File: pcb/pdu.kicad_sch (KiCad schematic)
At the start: 14 parts, among them J1 XT90-F, J2 XT90-M, J3 XT90-M, J4 XT90-F

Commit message: feat: ERC and DRC in CI
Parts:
- B1, B2: footprint PCM_kikit:Board -> kikit:Board; symbol PCM_kikit:Board -> kikit:Board
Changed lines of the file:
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@@
 	)
 	(symbol
-		(lib_id "PCM_kikit:Board")
+		(lib_id "kikit:Board")
 		(at 30.48 27.94 0)
 		(unit 1)
@@
 			)
 		)
-		(property "Footprint" "PCM_kikit:Board"
+		(property "Footprint" "kikit:Board"
 			(at 40.64 27.305 0)
 			(effects
@@
 	)
 	(symbol
-		(lib_id "PCM_kikit:Board")
+		(lib_id "kikit:Board")
 		(at 78.74 27.94 0)
 		(unit 1)
@@
 			)
 		)
-		(property "Footprint" "PCM_kikit:Board"
+		(property "Footprint" "kikit:Board"
 			(at 88.9 27.305 0)
 			(effects

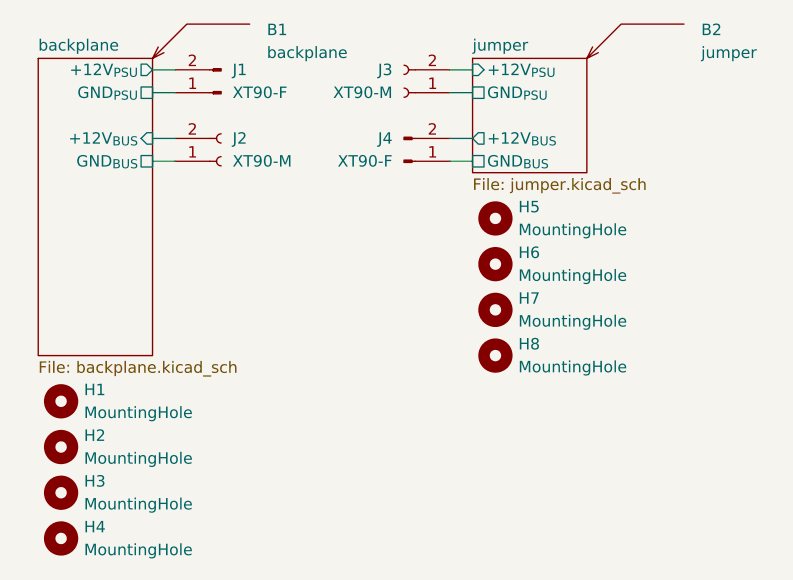
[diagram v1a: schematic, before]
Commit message: fix: ERC, mark edge connector pins as passive
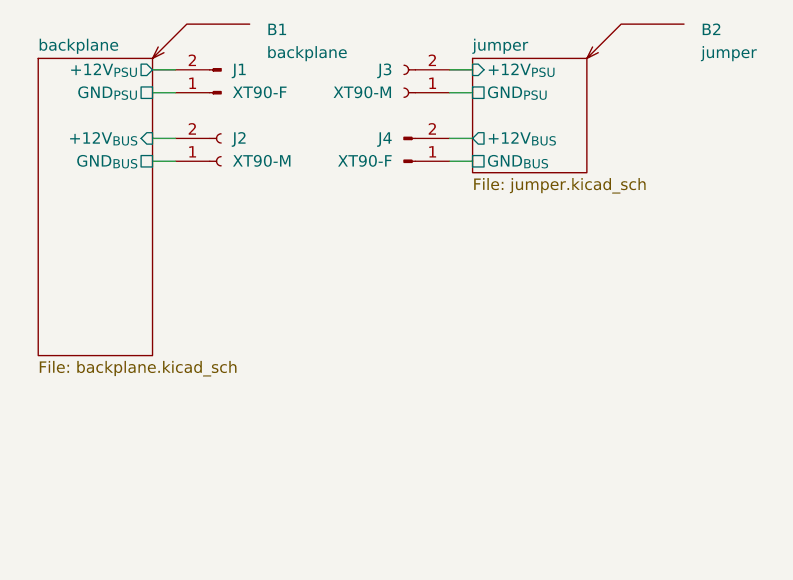
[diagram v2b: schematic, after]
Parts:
- removed H1, H2, H3, H4, H5, H6, H7, H8: MountingHole, MountingHole:MountingHole_3.2mm_M3, symbol Mechanical:MountingHole
